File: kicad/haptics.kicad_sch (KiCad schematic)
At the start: 7 parts, among them U501 DA7280

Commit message: Unfinished switch additions and fixes
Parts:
- TP501: value OUTP_TEST -> OUTP_PAD
- TP502: value OUTN_TEST -> OUTN_PAD
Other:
- note added: "Motor connected to TP pads"
- note removed: "Motor connected to TPs"
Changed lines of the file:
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@@
 		)
 	)
-	(text "Motor connected to TPs"
+	(text "Motor connected to TP pads"
 		(exclude_from_sim no)
 		(at 162.306 102.87 0)
@@
 			)
 		)
-		(property "Value" "OUTN_TEST"
+		(property "Value" "OUTN_PAD"
 			(at 152.908 109.22 90)
 			(effects
@@
 			)
 		)
-		(property "Value" "OUTP_TEST"
+		(property "Value" "OUTP_PAD"
 			(at 152.908 96.52 90)
 			(effects

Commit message: Part updates
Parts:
- TP501, TP502: footprint TestPoint:TestPoint_Pad_D1.5mm -> TestPoint:TestPoint_Pad_D1.0mm
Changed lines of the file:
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@@
 			)
 		)
-		(property "Footprint" "TestPoint:TestPoint_Pad_D1.5mm"
+		(property "Footprint" "TestPoint:TestPoint_Pad_D1.0mm"
 			(at 147.32 114.3 0)
 			(effects
@@
 			)
 		)
-		(property "Footprint" "TestPoint:TestPoint_Pad_D1.5mm"
+		(property "Footprint" "TestPoint:TestPoint_Pad_D1.0mm"
 			(at 147.32 101.6 0)
 			(effects

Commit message: Begin PCB, update footprints
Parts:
- C501: footprint Capacitor_SMD:C_0603_1608Metric_Pad1.08x0.95mm_HandSolder -> Capacitor_SMD:C_0402_1005Metric
- R501, R502, R503: footprint Resistor_SMD:R_0603_1608Metric_Pad0.98x0.95mm_HandSolder -> Resistor_SMD:R_0402_1005Metric
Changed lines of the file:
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@@
 			)
 		)
-		(property "Footprint" "Capacitor_SMD:C_0603_1608Metric_Pad1.08x0.95mm_HandSolder"
+		(property "Footprint" "Capacitor_SMD:C_0402_1005Metric"
 			(at 125.4252 125.73 0)
 			(effects
@@
 			)
 		)
-		(property "Footprint" "Resistor_SMD:R_0603_1608Metric_Pad0.98x0.95mm_HandSolder"
+		(property "Footprint" "Resistor_SMD:R_0402_1005Metric"
 			(at 103.632 95.25 90)
 			(effects
@@
 			)
 		)
-		(property "Footprint" "Resistor_SMD:R_0603_1608Metric_Pad0.98x0.95mm_HandSolder"
+		(property "Footprint" "Resistor_SMD:R_0402_1005Metric"
 			(at 112.522 92.71 90)
 			(effects
@@
 			)
 		)
-		(property "Footprint" "Resistor_SMD:R_0603_1608Metric_Pad0.98x0.95mm_HandSolder"
+		(property "Footprint" "Resistor_SMD:R_0402_1005Metric"
 			(at 123.952 88.9 90)
 			(effects

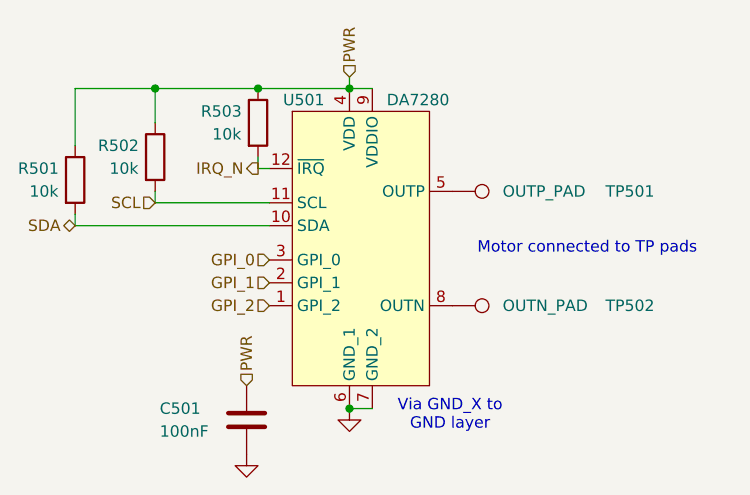
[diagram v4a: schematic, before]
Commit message: Finish PCB component placement
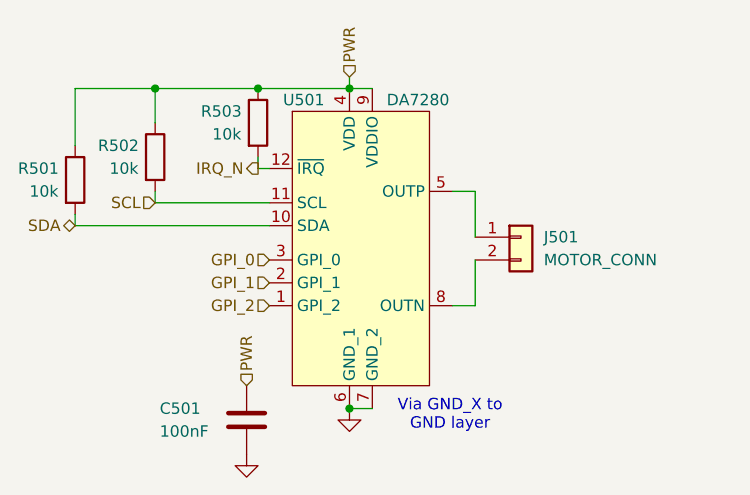
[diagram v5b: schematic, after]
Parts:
- removed TP501: OUTP_PAD, TestPoint:TestPoint_Pad_D1.0mm, symbol Connector:TestPoint
- removed TP502: OUTN_PAD, TestPoint:TestPoint_Pad_D1.0mm, symbol Connector:TestPoint
- added J501: MOTOR_CONN, Raven:CUSTOM_MOTOR_CONN, symbol Connector_Generic:Conn_01x02
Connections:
- net at U501.8 (OUTN): now also J501.2 (Pin_2)
- net at U501.5 (OUTP): now also J501.1 (Pin_1)
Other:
- note removed: "Motor connected to TP pads"
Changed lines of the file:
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@@
+	(wire
+		(pts
+			(xy 149.86 104.14) (xy 149.86 109.22)
+		)
+		(stroke
+			(width 0)
+			(type default)
+		)
+	)
 	(wire
 		(pts
@@
 	(wire
 		(pts
+			(xy 149.86 101.6) (xy 149.86 96.52)
+		)
+		(stroke
+			(width 0)
+			(type default)
+		)
+	)
+	(wire
+		(pts
+			(xy 149.86 96.52) (xy 147.32 96.52)
+		)
+		(stroke
+			(width 0)
+			(type default)
+		)
+	)
+	(wire
+		(pts
 			(xy 114.3 85.09) (xy 125.73 85.09)
 		)
@@
 		(pts
 			(xy 114.3 96.52) (xy 114.3 97.79)
+		)
+		(stroke
+			(width 0)
+			(type default)
+		)
+	)
+	(wire
+		(pts
+			(xy 149.86 109.22) (xy 147.32 109.22)
 		)
 		(stroke
@@
 		)
 	)
-	(text "Motor connected to TP pads"
-		(exclude_from_sim no)
-		(at 162.306 102.87 0)
-		(effects
-			(font
-				(size 1.27 1.27)
-			)
-		)
-	)
 	(hierarchical_label "IRQ_N"
 		(shape output)
@@
 			)
 			(justify right)
-		)
-	)
-	(symbol
-		(lib_id "Connector:TestPoint")
-		(at 147.32 109.22 270)
-		(unit 1)
-		(exclude_from_sim no)
-		(in_bom yes)
-		(on_board yes)
-		(dnp no)
-		(property "Reference" "TP502"
-			(at 164.338 109.22 90)
-			(effects
-				(font
-					(size 1.27 1.27)
-				)
-				(justify left)
-			)
-		)
-		(property "Value" "OUTN_PAD"
-			(at 152.908 109.22 90)
-			(effects
-				(font
-					(size 1.27 1.27)
-				)
-				(justify left)
-			)
-		)
-		(property "Footprint" "TestPoint:TestPoint_Pad_D1.0mm"
-			(at 147.32 114.3 0)
-			(effects
-				(font
-					(size 1.27 1.27)
-				)
-				(hide yes)
-			)
-		)
-		(property "Datasheet" "~"
-			(at 147.32 114.3 0)
-			(effects
-				(font
-					(size 1.27 1.27)
-				)
-				(hide yes)
-			)
-		)
-		(property "Description" "test point"
-			(at 147.32 109.22 0)
-			(effects
-				(font
-					(size 1.27 1.27)
-				)
-				(hide yes)
-			)
-		)
-		(property "JLC" "XXXXXX"
-			(at 147.32 109.22 0)
-			(effects
-				(font
-					(size 1.27 1.27)
-				)
-				(hide yes)
-			)
-		)
-		(property "LCSC" "XXXXXX"
-			(at 147.32 109.22 0)
-			(effects
-				(font
-					(size 1.27 1.27)
-				)
-				(hide yes)
-			)
-		)
-		(pin "1"
-		)
-		(instances
-			(project "kicad"
-				(path "/97e37379-fec6-4f0d-82d9-4ea53516bb02/6e1279b2-387a-4a79-8fd5-6fdc8d551df2"
-					(reference "TP502")
-					(unit 1)
-				)
-			)
-		)
-	)
-	(symbol
-		(lib_id "Connector:TestPoint")
-		(at 147.32 96.52 270)
-		(unit 1)
-		(exclude_from_sim no)
-		(in_bom yes)
-		(on_board yes)
-		(dnp no)
-		(property "Reference" "TP501"
-			(at 164.338 96.52 90)
-			(effects
-				(font
-					(size 1.27 1.27)
-				)
-				(justify left)
-			)
-		)
-		(property "Value" "OUTP_PAD"
-			(at 152.908 96.52 90)
-			(effects
-				(font
-					(size 1.27 1.27)
-				)
-				(justify left)
-			)
-		)
-		(property "Footprint" "TestPoint:TestPoint_Pad_D1.0mm"
-			(at 147.32 101.6 0)
-			(effects
-				(font
-					(size 1.27 1.27)
-				)
-				(hide yes)
-			)
-		)
-		(property "Datasheet" "~"
-			(at 147.32 101.6 0)
-			(effects
-				(font
-					(size 1.27 1.27)
-				)
-				(hide yes)
-			)
-		)
-		(property "Description" "test point"
-			(at 147.32 96.52 0)
-			(effects
-				(font
-					(size 1.27 1.27)
-				)
-				(hide yes)
-			)
-		)
-		(property "JLC" "XXXXXX"
-			(at 147.32 96.52 0)
-			(effects
-				(font
-					(size 1.27 1.27)
-				)
-				(hide yes)
-			)
-		)
-		(property "LCSC" "XXXXXX"
-			(at 147.32 96.52 0)
-			(effects
-				(font
-					(size 1.27 1.27)
-				)
-				(hide yes)
-			)
-		)
-		(pin "1"
-		)
-		(instances
-			(project "kicad"
-				(path "/97e37379-fec6-4f0d-82d9-4ea53516bb02/6e1279b2-387a-4a79-8fd5-6fdc8d551df2"
-					(reference "TP501")
-					(unit 1)
-				)
-			)
 		)
 	)
@@
 					(unit 1)
 				)
+			)
+		)
+	)
+	(symbol
+		(lib_id "Connector_Generic:Conn_01x02")
+		(at 154.94 101.6 0)
+		(unit 1)
+		(exclude_from_sim no)
+		(in_bom yes)
+		(on_board yes)
+		(dnp no)
+		(fields_autoplaced yes)
+		(property "Reference" "J501"
+			(at 157.48 101.5999 0)
+			(effects
+				(font
+					(size 1.27 1.27)
+				)
+				(justify left)
+			)
+		)
+		(property "Value" "MOTOR_CONN"
+			(at 157.48 104.1399 0)
+			(effects
+				(font
+					(size 1.27 1.27)
+				)
+				(justify left)
+			)
+		)
+		(property "Footprint" "Raven:CUSTOM_MOTOR_CONN"
+			(at 154.94 101.6 0)
+			(effects
+				(font
+					(size 1.27 1.27)
+				)
+				(hide yes)
+			)
+		)
+		(property "Datasheet" "~"
+			(at 154.94 101.6 0)
+			(effects
+				(font
+					(size 1.27 1.27)
+				)
+				(hide yes)
+			)
+		)
+		(property "Description" "Generic connector, single row, 01x02, script generated (kicad-library-utils/schlib/autogen/connector/)"
+			(at 154.94 101.6 0)
+			(effects
+				(font
+					(size 1.27 1.27)
+				)
+				(hide yes)
+			)
+		)
+		(pin "2"
+		)
+		(pin "1"
+		)
+		(instances
+			(project "kicad"
+				(path "/97e37379-fec6-4f0d-82d9-4ea53516bb02/6e1279b2-387a-4a79-8fd5-6fdc8d551df2"
+					(reference "J501")
+					(unit 1)
+				)
